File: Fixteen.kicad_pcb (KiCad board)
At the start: 2 copper layers, 34.2 x 62.7 mm, 16 parts, among them J1 TED_SOCKET, J2 RAM_SELECTOR, J99 OSHW_LOGO, U1 MOS_7360_TED, U2 74LS257, U3 74LS257, U4 4464, U5 4464, U6 DT1042, U7 DT1042

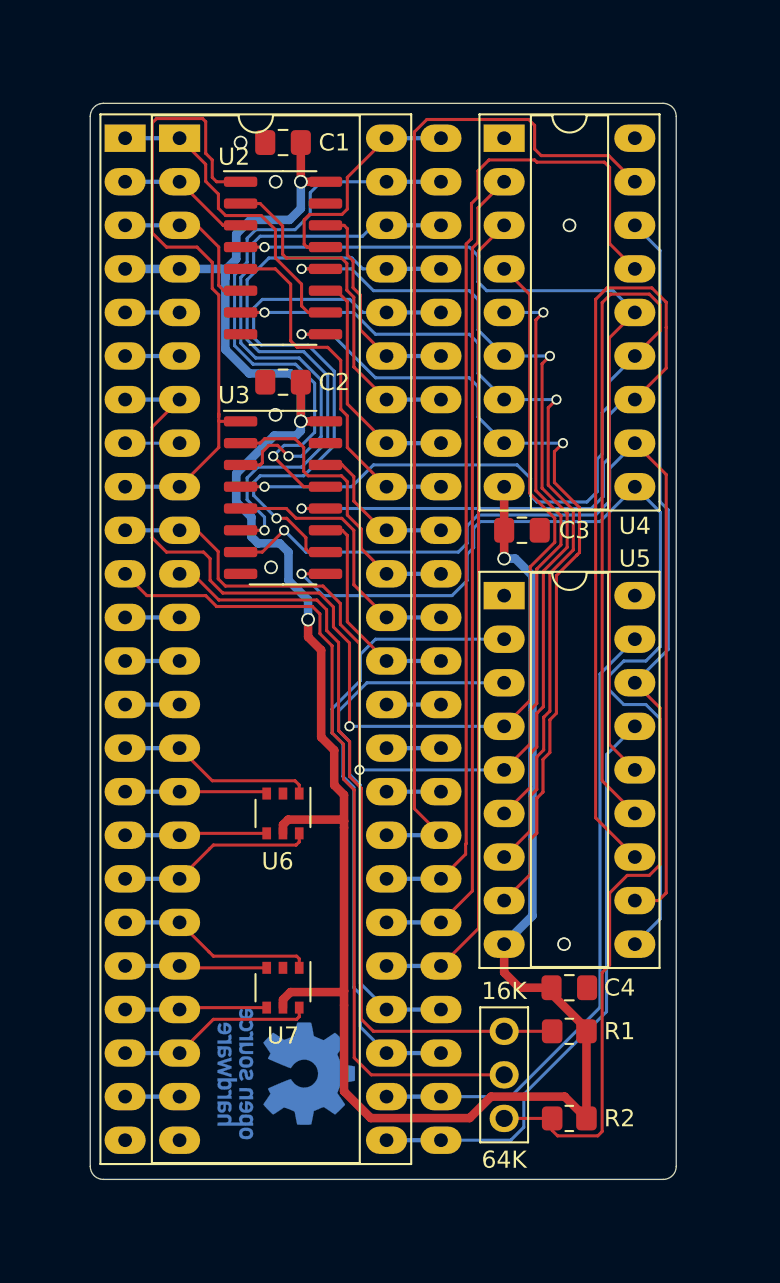
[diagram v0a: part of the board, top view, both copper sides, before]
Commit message: Redo connections as they are on OpenC16RamExpansion V2 did not work :(
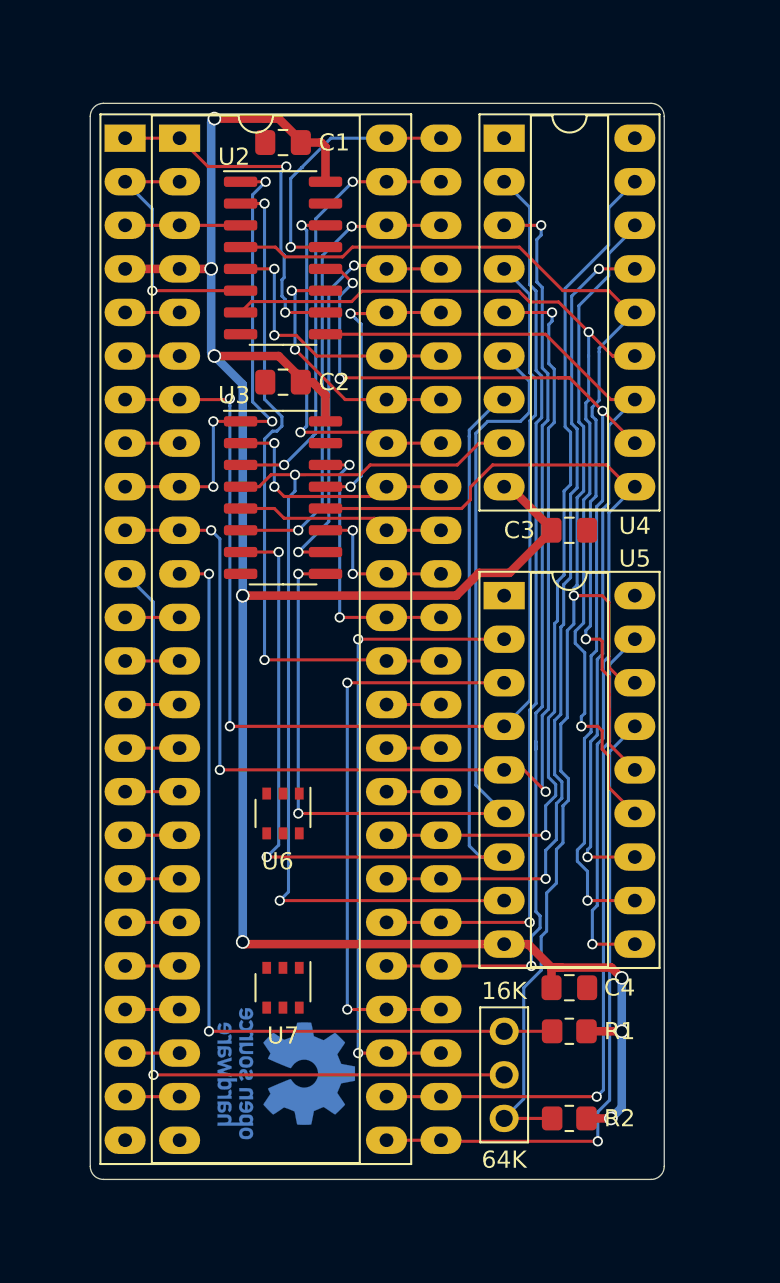
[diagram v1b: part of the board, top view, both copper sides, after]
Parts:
- moved C3 2.76 mm to (147.8, 98.8)
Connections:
- U2 pad 11: a10 -> a9
- U2 pad 12: /64K RAM Expansion/m6 -> /64K RAM Expansion/m3
- U2 pad 14: a8 -> a10
- U2 pad 2: a9 -> a15
- U2 pad 3: a1 -> a0
- U2 pad 5: a11 -> a8
- U2 pad 6: a0 -> a1
- U2 pad 7: /64K RAM Expansion/m5 -> /64K RAM Expansion/m1
- U2 pad 9: /64K RAM Expansion/m4 -> /64K RAM Expansion/m2
- U3 pad 10: a7 -> a6
- U3 pad 11: a15 -> a13
- U3 pad 12: /64K RAM Expansion/m2 -> /64K RAM Expansion/m7
- U3 pad 13: a4 -> a7
- U3 pad 14: a12 -> a14
- U3 pad 2: a13 -> a11
- U3 pad 3: a5 -> a4
- U3 pad 4: /64K RAM Expansion/m1 -> /64K RAM Expansion/m4
- U3 pad 5: a14 -> a12
- U3 pad 6: a6 -> a5
- U3 pad 7: /64K RAM Expansion/m3 -> /64K RAM Expansion/m5
- U3 pad 9: /64K RAM Expansion/m7 -> /64K RAM Expansion/m6
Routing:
- net a15: track 12.8 -> 39.3 mm, vias 0 -> 2
- net /64K RAM Expansion/m2: track 70.7 -> 50.2 mm
- net a7: track 35.3 -> 17.4 mm, vias 1 -> 2
- net /64K RAM Expansion/m5: track 50.7 -> 63.5 mm
- net /64K RAM Expansion/m1: track 69.9 -> 57.1 mm, vias 1 -> 2
- net VCC: track 144.6 -> 132.3 mm, vias 4 -> 8
- net d6: track 60.0 -> 49.0 mm, vias 0 -> 2
- net d7: track 60.9 -> 50.1 mm, vias 0 -> 1
- net a6: track 35.4 -> 24.8 mm, vias 1 -> 2
- net /64K RAM Expansion/m6: track 48.0 -> 57.9 mm
- net a4: track 35.2 -> 25.8 mm, vias 1 -> 2
- net SEL: track 37.9 -> 28.6 mm, vias 0 -> 4
- net a13: track 17.9 -> 9.27 mm, vias 0 -> 2
- net /k7: track 11.6 -> 3.17 mm
- net /k4: track 11.6 -> 3.17 mm
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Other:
- board size 34.2 x 62.7 mm -> 33.5 x 62.7 mm

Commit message: Ready for V3
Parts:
- removed J99: OSHW_LOGO, Symbol:OSHW-Logo_7.5x8mm_Copper
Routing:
- net /k4: track 3.17 -> 11.3 mm
- net /k3: track 3.17 -> 11.3 mm
- net /k7: track 3.17 -> 11.3 mm
- net /k0: track 3.17 -> 11.3 mm
- net /k6: track 3.17 -> 8.30 mm
- net /k5: track 3.17 -> 8.30 mm
- net /k2: track 3.17 -> 8.30 mm
- net /k1: track 3.17 -> 8.30 mm
- net ~RAS: track 70.0 -> 65.2 mm, vias 4 -> 3
- net /~cas: track 50.3 -> 45.8 mm
- net /~cas_16k: track 48.4 -> 43.9 mm, vias 2 -> 1
- net VCC: track 132.3 -> 135.2 mm, vias 8 -> 9
- net a15: track 39.3 -> 36.9 mm
- net /64K RAM Expansion/m5: track 63.5 -> 61.1 mm
- net R_~W: track 69.4 -> 67.2 mm, vias 2 -> 1
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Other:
- board text added: "Fixteen V3"
- board text removed: "V2"
- board text removed: "github.com/SukkoPera/Fixteen Licensed under CERN OHL v.1.2"

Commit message: Finalize release
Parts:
- added J99: OSHW_LOGO, Symbol:OSHW-Logo_5.7x6mm_Copper, B.Cu at (131.1, 131.8)

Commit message: Add license statement, project URL and version number
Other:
- board text added: "Licensed under CERN OHL v.1.2"
- board text added: "V3"
- board text added: "https://github.com/SukkoPera/Fixteen"
- board text removed: "Fixteen V3"
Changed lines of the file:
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@@
   (general
     (thickness 1.6)
-    (drawings 15)
+    (drawings 17)
     (tracks 684)
     (zones 0)
@@
     (rev 3git)
     (company SukkoPera)
-    (comment 1 "Licensed under CERN OHL v.1.2")
+    (comment 1 https://github.com/SukkoPera/Fixteen)
+    (comment 2 "Licensed under CERN OHL v.1.2")
   )
   (layers
@@
       (xy 0.376964 2.709982)) (layer B.Cu) (width 0.01))
   )
+  (gr_text V3 (at 151.892 134.874 270) (layer B.SilkS)
+    (effects (font (size 1 1) (thickness 0.15)) (justify mirror))
+  )
+  (gr_text "Licensed under CERN OHL v.1.2" (at 146.7505 87.316238 270) (layer B.SilkS)
+    (effects (font (size 1 1) (thickness 0.15)) (justify mirror))
+  )
+  (gr_text https://github.com/SukkoPera/Fixteen (at 149.0405 90.101952 270) (layer B.SilkS)
+    (effects (font (size 1 1) (thickness 0.15)) (justify mirror))
+  )
   (gr_text 16K (at 144.018 125.6665) (layer F.SilkS)
     (effects (font (size 1 1) (thickness 0.15)))
@@
     (effects (font (size 1 1) (thickness 0.15)))
   )
-  (gr_text "Fixteen V3" (at 128.8415 117.983 -90) (layer B.Mask)
-    (effects (font (size 1.6 1.6) (thickness 0.25)) (justify mirror))
-  )
   (gr_line (start 118.11 101.346) (end 118.11 108.966) (layer F.Fab) (width 0.15))
